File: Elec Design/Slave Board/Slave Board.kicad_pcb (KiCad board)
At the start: 2 copper layers, 81.3 x 358.6 mm, 86 parts, among them J1 JTAG, J2 OSTTC020162, J3 OSTTC030162, J4 OSTTC020162, J5 OSTTC030162, J6 0022232041, M1 VID28-05, M2 VID28-05, M3 VID28-05, M4 VID28-05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

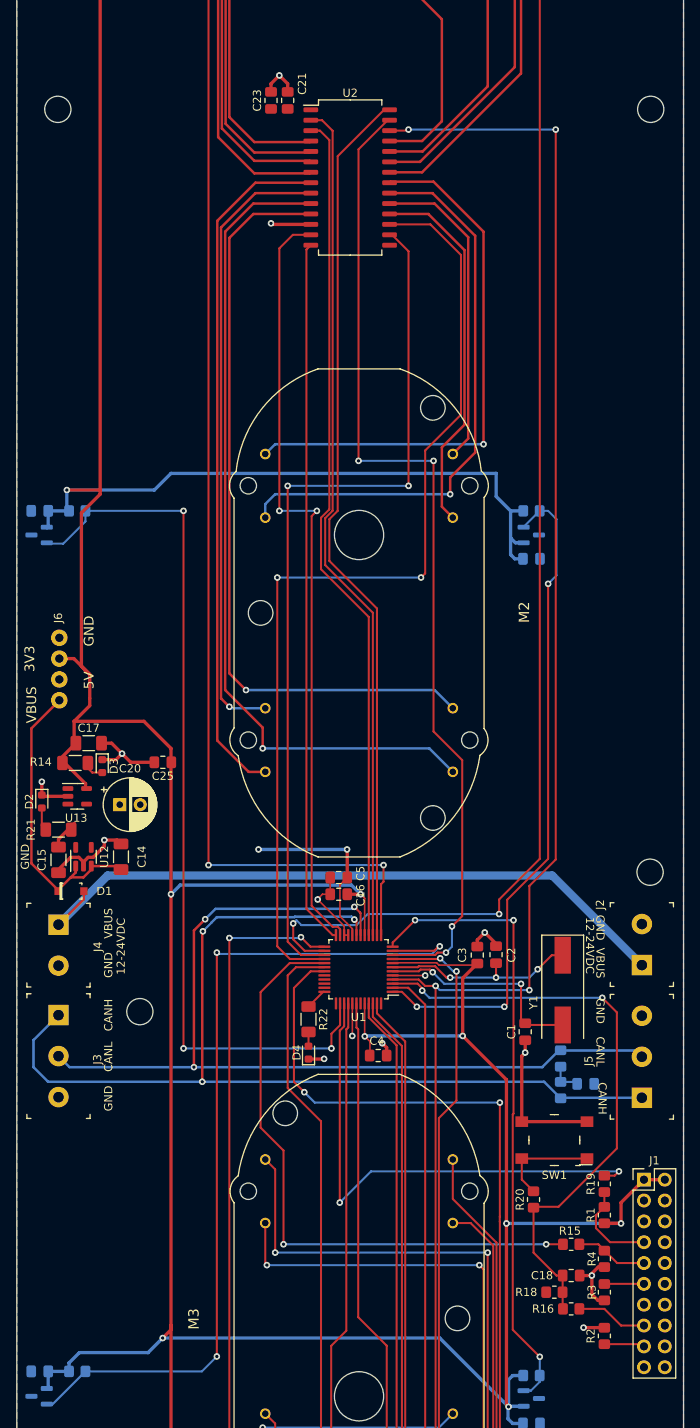
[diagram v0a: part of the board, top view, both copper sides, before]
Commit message: slave board changes. changed jtag port and power supply
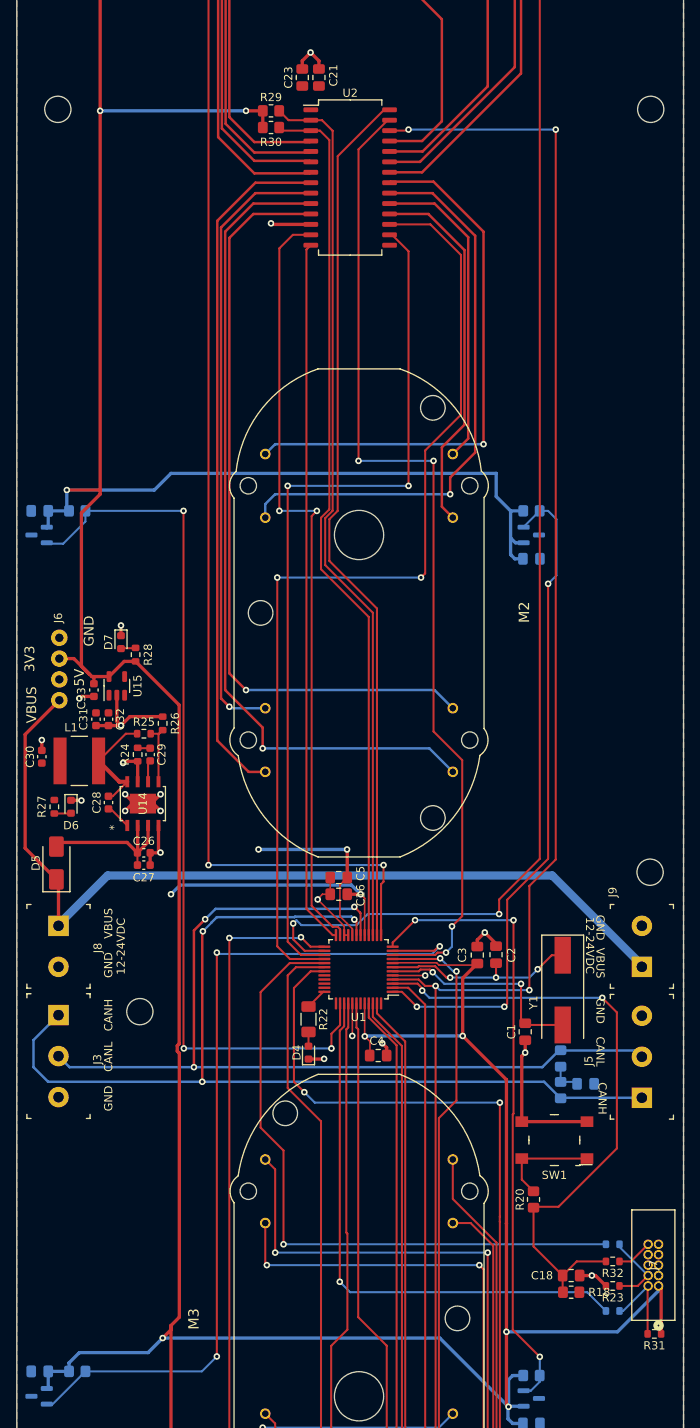
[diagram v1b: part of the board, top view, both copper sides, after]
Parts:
- removed C14, C15, C17: 10uF, Capacitor_SMD:C_1206_3216Metric_Pad1.33x1.80mm_HandSolder
- removed C20: 47uF, Capacitor_THT:CP_Radial_D6.3mm_P2.50mm
- removed C25: 100nF, Capacitor_SMD:C_0805_2012Metric_Pad1.18x1.45mm_HandSolder
- removed D1: 1N5819HW-7-F, digikey-footprints:SOD-123
- removed D2, D3: LED Low current, LED_SMD:LED_0603_1608Metric
- removed J1: JTAG, Connector_PinHeader_2.54mm:PinHeader_2x10_P2.54mm_Vertical
- removed J2, J4: OSTTC020162, digikey-footprints:Term_Block_1x2_P5mm
- removed R1, R2, R3, R4: 10k, Resistor_SMD:R_0805_2012Metric_Pad1.20x1.40mm_HandSolder
- removed R14: 750R, Resistor_SMD:R_1206_3216Metric_Pad1.30x1.75mm_HandSolder
- removed R15, R16, R19: 50R, Resistor_SMD:R_0805_2012Metric_Pad1.20x1.40mm_HandSolder
- removed R21: 1k6, Resistor_SMD:R_1206_3216Metric_Pad1.30x1.75mm_HandSolder
- removed U12: NCP718xSN500, Package_TO_SOT_SMD:SOT-23-5
- removed U13: NCP718xSN330, Package_TO_SOT_SMD:SOT-23-5
- added C26: 10uF, Capacitor_SMD:C_0603_1608Metric, F.Cu at (218.7, 191.0)
- added C27: 0.1uF, Capacitor_SMD:C_0603_1608Metric, F.Cu at (218.7, 192.5)
- added C28: 0.1uF, Capacitor_SMD:C_0603_1608Metric, F.Cu at (214.4, 184.9)
- added C29: 6800pF, Capacitor_SMD:C_0603_1608Metric, F.Cu at (219.5, 179.1)
- added C30: 22uF, Capacitor_SMD:C_0603_1608Metric, F.Cu at (206.2, 179.3)
- added C31: 22uF, Capacitor_SMD:C_0603_1608Metric, F.Cu at (212.9, 174.8)
- added C32: 1uF, Capacitor_SMD:C_0603_1608Metric, F.Cu at (214.4, 174.8)
- added C33: 1uF, Capacitor_SMD:C_0603_1608Metric, F.Cu at (212.6, 171.2)
- added D5: B340, Diode_SMD:D_SMA, F.Cu at (208.0, 192.3)
- added D6: LED Low current, LED_SMD:LED_0603_1608Metric, F.Cu at (209.8, 185.4)
- added D7: LED Low current, LED_SMD:LED_0603_1608Metric, F.Cu at (215.9, 165.4)
- added J7: Conn_ARM_JTAG_SWD_10, 10 pin jtag:CONN_3220-10-0100-00_CNC, F.Cu at (281.4, 243.8)
- added J8: OSTTC020162, digikey-footprints:Term_Block_1x2_P5mm, F.Cu at (208.3, 199.9)
- added J9: OSTTC020162, digikey-footprints:Term_Block_1x2_P5mm, F.Cu at (279.4, 204.9)
- added L1: 4.7uH, NR6028T4R7M:IND_NR6028T4R7M, F.Cu at (210.8, 179.8)
- added R23: 10k, Resistor_SMD:R_0603_1608Metric, F.Cu at (275.8, 243.8)
- added R24: 10k, Resistor_SMD:R_0603_1608Metric, F.Cu at (217.9, 179.1)
- added R25: 430k, Resistor_SMD:R_0603_1608Metric, F.Cu at (218.7, 176.5)
- added R26: 82k, Resistor_SMD:R_0603_1608Metric, F.Cu at (221.0, 175.3)
- added R27: 1k6, Resistor_SMD:R_0603_1608Metric, F.Cu at (207.8, 185.4)
- added R28: 750R, Resistor_SMD:R_0603_1608Metric, F.Cu at (217.7, 166.9)
- added R29: 10k, Resistor_SMD:R_0805_2012Metric_Pad1.20x1.40mm_HandSolder, F.Cu at (234.2, 100.6)
- added R30: 10k, Resistor_SMD:R_0805_2012Metric_Pad1.20x1.40mm_HandSolder, F.Cu at (234.2, 102.6)
- added R31: 10k, Resistor_SMD:R_0603_1608Metric, F.Cu at (280.9, 249.7)
- added R32: 50R, Resistor_SMD:R_0603_1608Metric, F.Cu at (275.8, 240.9)
- added R33: 50R, Resistor_SMD:R_0603_1608Metric, B.Cu at (275.8, 238.8)
- added R34: 50R, Resistor_SMD:R_0603_1608Metric, B.Cu at (275.8, 246.9)
- added U14: BD9E302EFJ-E2, BD9E302EFJ-E2:HTSOP-J8_ROM, F.Cu at (218.6, 185.0)
- added U15: NCP718xSN330, Package_TO_SOT_SMD:SOT-23-5, F.Cu at (215.4, 170.7)
- R20: value 100k -> 100R
- moved C21 4.72 mm to (240.0, 96.5)
- moved C23 4.72 mm to (238.0, 96.5)
- moved R18 2.05 mm to (270.8, 244.6), turned to 180 degrees
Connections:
- C18 pad 2: Net-(C18-Pad2) -> /RESET
- R18 pad 2: Net-(C18-Pad2) -> /RESET
- R20 pad 1: Net-(C18-Pad2) -> /RESET
- U1 pad 3: Net-(C18-Pad2) -> /RESET
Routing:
- net Net-(D1-PadA): track 83.6 -> 0.00 mm
- net VBUS: track 36.2 -> 109.5 mm
- net Net-(C18-Pad2): track 73.0 -> 0.00 mm, vias 2 -> 0
- net /RESET: track 8.95 -> 76.5 mm, vias 0 -> 2
- net Net-(D5-A): track 0.00 -> 19.1 mm
- net +3.3V: track 793.5 -> 808.3 mm, vias 11 -> 12
- net Net-(U14-SW): track 0.00 -> 13.6 mm
- net Net-(J1-Pad7): track 11.4 -> 0.00 mm
- net Net-(J7-SWDIO/TMS): track 0.00 -> 10.6 mm
- net Net-(J7-SWDCLK/TCK): track 0.00 -> 9.28 mm
- net Net-(J1-Pad9): track 8.82 -> 0.00 mm
- net Net-(U14-FB): track 0.00 -> 8.14 mm
- net GND: track 97.7 -> 105.1 mm, vias 16 -> 23
- net /SWDIO: track 62.1 -> 68.1 mm, vias 2 -> 1
- net Net-(J1-Pad17): track 5.45 -> 0.00 mm
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
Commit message: pcb cleanup
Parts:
- M1, M2, M3, M4: value VID28-05 -> Val**
- moved C30 6.36 mm to (206.5, 185.7), turned to -90 degrees
- moved C31 1.85 mm to (211.1, 175.3), turned to 0 degrees
- moved R27 1.80 mm to (209.6, 185.7)
- moved D6 1.80 mm to (211.6, 185.7)
- moved J6 1.12 mm to (207.3, 164.8)
- moved C32 0.57 mm to (214.1, 175.3), turned to 180 degrees
- moved C28 0.36 mm to (214.6, 185.2)
- moved L1 0.25 mm to (210.8, 180.1)
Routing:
- net +3.3V: track 808.3 -> 812.8 mm
- net /HAll B Min - 1: track 108.5 -> 109.6 mm
- net GND: track 105.1 -> 104.4 mm, vias 23 -> 24
- net VBUS: track 109.5 -> 110.1 mm

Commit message: further board cleanup, getting ready for production
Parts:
- moved R31 0.76 mm to (280.9, 250.4)
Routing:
- net /HAll A Min - 1 : track 199.7 -> 196.8 mm
- net Net-(J7-SWDIO/TMS): track 10.6 -> 11.4 mm
- net +3.3V: track 812.8 -> 813.5 mm
